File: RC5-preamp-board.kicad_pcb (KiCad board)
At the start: 2 copper layers, 69.8 x 48.3 mm, 28 parts, among them P1 RAW_DC, P10 CTL_OUT, P2 VCC, P201 FTDI Basic, P3 VCC, P4 VCC, P5 VCC, P6 VCC, P7 VCC, P8 INPUTS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

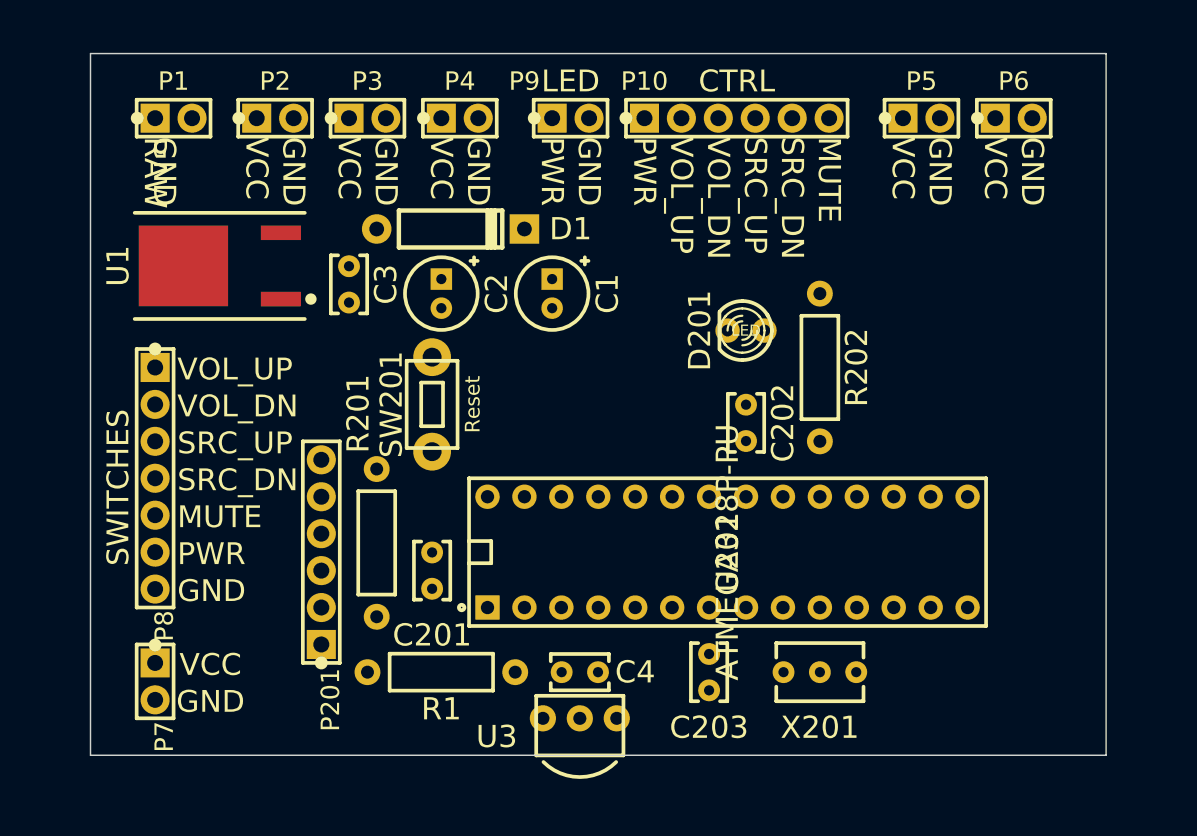
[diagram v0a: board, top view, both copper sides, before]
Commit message: Dimensioned and routed.
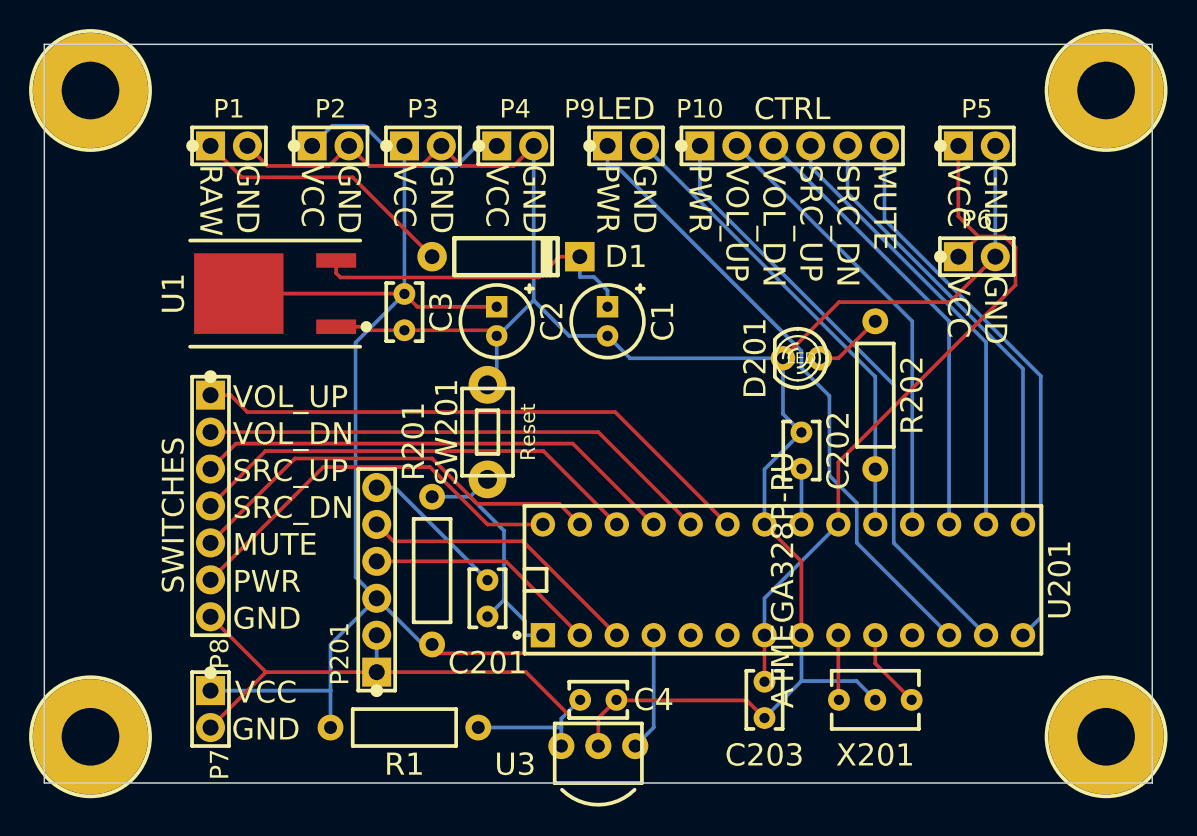
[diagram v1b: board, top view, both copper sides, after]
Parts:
- added mtg1: 4-40-PTH, mfk-MTG_4-40_0.156x0.312in, F.Cu at (104.8, 87.0)
- added mtg2: 4-40-PTH, mfk-MTG_4-40_0.156x0.312in, F.Cu at (174.6, 87.0)
- added mtg3: 4-40-PTH, mfk-MTG_4-40_0.156x0.312in, F.Cu at (174.6, 131.4)
- added mtg4: 4-40-PTH, mfk-MTG_4-40_0.156x0.312in, F.Cu at (104.8, 131.4)
- moved P6 9.86 mm to (165.7, 98.4)
- moved R1 4.58 mm to (126.4, 130.8)
- moved R201 4.26 mm to (128.3, 120.0)
- moved C1 4.26 mm to (140.3, 102.9)
- moved C2 4.26 mm to (132.7, 102.9)
- moved C201 4.26 mm to (132.1, 121.9)
- moved C203 4.26 mm to (151.1, 128.9)
- moved D1 4.26 mm to (133.3, 98.4)
- moved P1 4.26 mm to (114.3, 90.8)
- moved P10 4.26 mm to (153.0, 90.8)
- moved P2 4.26 mm to (121.3, 90.8)
- moved P3 4.26 mm to (127.6, 90.8)
- moved P4 4.26 mm to (134.0, 90.8)
- moved P5 4.26 mm to (165.7, 90.8)
- moved P9 4.26 mm to (141.6, 90.8)
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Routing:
- net DGND: track 0.00 -> 182.1 mm
- net /arduino-pcb/V_VCC: track 0.00 -> 161.0 mm
- net /arduino-pcb/D6: track 0.00 -> 43.7 mm
- net /arduino-pcb/D7: track 0.00 -> 41.8 mm
- net /arduino-pcb/A0: track 0.00 -> 39.2 mm
- net /arduino-pcb/D8: track 0.00 -> 38.6 mm
- net /arduino-pcb/A1: track 0.00 -> 35.7 mm
- net /arduino-pcb/A2: track 0.00 -> 33.5 mm
- net /arduino-pcb/SCK: track 0.00 -> 32.6 mm
- net /arduino-pcb/A3: track 0.00 -> 31.6 mm
- net /arduino-pcb/MOSI: track 0.00 -> 31.0 mm
- net /arduino-pcb/MISO: track 0.00 -> 31.0 mm
- net /arduino-pcb/D9: track 0.00 -> 31.0 mm
- net /arduino-pcb/D10: track 0.00 -> 31.0 mm
- net /arduino-pcb/A4: track 0.00 -> 29.7 mm
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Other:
- board size 69.8 x 48.3 mm -> 76.2 x 50.8 mm

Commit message: Shrunk and routed.
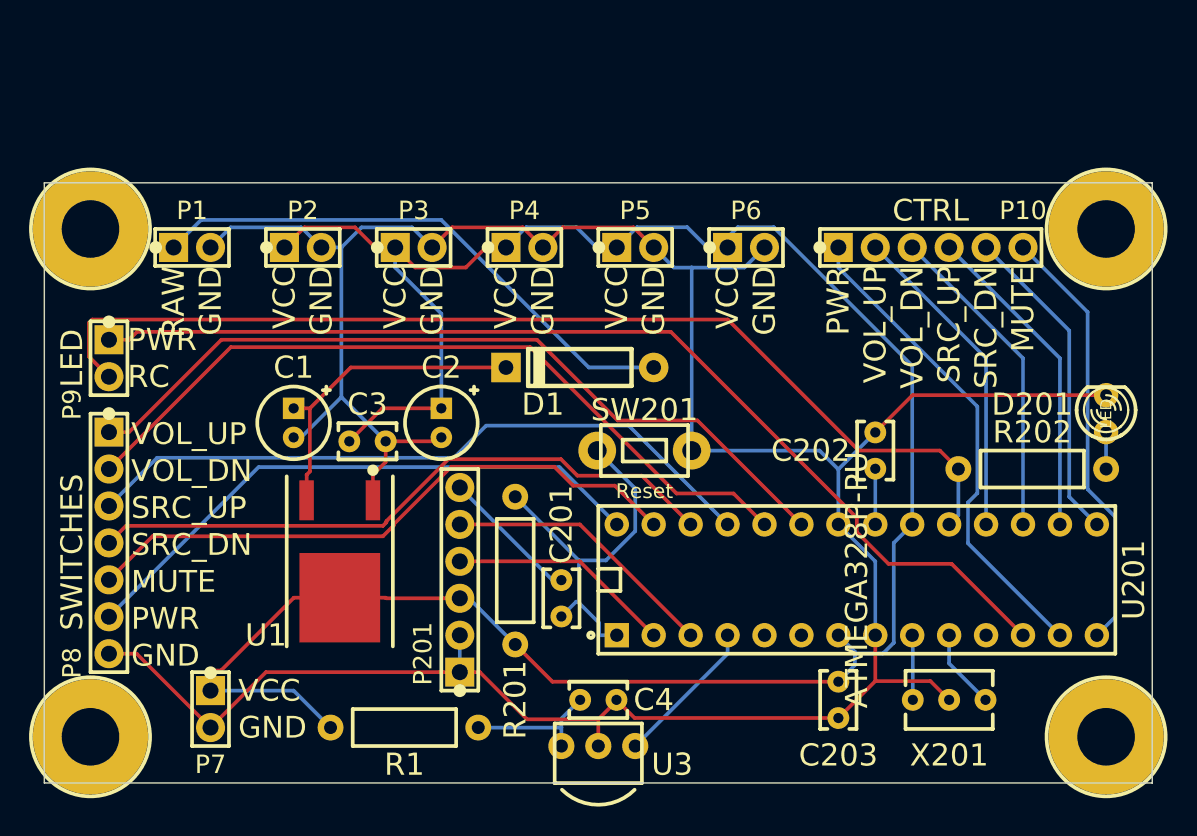
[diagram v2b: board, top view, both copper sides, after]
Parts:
- moved P9 38.4 mm to (106.0, 105.4), turned to 270 degrees
- moved P5 24.5 mm to (142.2, 97.8)
- moved C1 22.7 mm to (118.7, 109.9)
- moved D201 21.3 mm to (174.6, 109.2), turned to 90 degrees
- moved U1 18.9 mm to (121.9, 119.4), turned to 270 degrees
- moved P6 15.9 mm to (149.9, 97.8)
- moved R202 11.9 mm to (169.5, 113.0), turned to 0 degrees
- moved P10 11.8 mm to (162.6, 97.8)
- moved SW201 10.9 mm to (142.9, 111.8), turned to 0 degrees
- moved mtg1 9.52 mm to (104.8, 96.5)
- moved mtg2 9.52 mm to (174.6, 96.5)
- moved C3 9.25 mm to (123.8, 111.1), turned to 0 degrees
- moved D1 9.16 mm to (138.4, 106.0), turned to 180 degrees
- moved C2 7.96 mm to (128.9, 109.9)
- moved P8 7.43 mm to (106.0, 118.1)
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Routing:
- net /arduino-pcb/SCK: track 32.6 -> 72.5 mm
- net /arduino-pcb/D6: track 43.7 -> 72.3 mm
- net /RAW_DC: track 18.4 -> 38.0 mm
- net DGND: track 182.1 -> 200.4 mm
- net /arduino-pcb/A1: track 35.7 -> 53.6 mm
- net /arduino-pcb/A0: track 39.2 -> 55.5 mm
- net /arduino-pcb/A2: track 33.5 -> 47.6 mm
- net /arduino-pcb/A5: track 27.7 -> 40.8 mm
- net /arduino-pcb/A3: track 31.6 -> 44.3 mm
- net /arduino-pcb/A4: track 29.7 -> 42.4 mm
- net /arduino-pcb/D10: track 31.0 -> 22.2 mm
- net /arduino-pcb/MOSI: track 31.0 -> 22.2 mm
- net /arduino-pcb/MISO: track 31.0 -> 22.2 mm
- net /arduino-pcb/D9: track 31.0 -> 22.2 mm
- net /arduino-pcb/D8: track 38.6 -> 29.8 mm
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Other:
- board size 76.2 x 50.8 mm -> 76.2 x 41.3 mm
- board text added: "RC"

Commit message: Removed one VCC tap. Keystone 621 mtg added. Routed.
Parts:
- removed P7: VCC, mfk-SIL-2
- added VAL: REF, oshw-logo-150mil-FSilk, F.Cu at (144.8, 120.7)
- mtg1, mtg2, mtg3, mtg4: value 4-40-PTH -> 621; footprint mfk-MTG_4-40_0.156x0.312in -> mfk-KEYSTONE-621
- moved mtg3 69.8 mm to (104.8, 131.4)
- moved mtg4 69.8 mm to (174.6, 131.4)
- moved P6 49.0 mm to (113.0, 130.2), turned to 270 degrees
- moved D1 19.7 mm to (118.7, 105.4), turned to 0 degrees
- moved P2 3.81 mm to (123.2, 97.8)
- moved P3 3.81 mm to (130.8, 97.8)
- moved P4 3.81 mm to (138.4, 97.8)
- moved P5 3.81 mm to (146.1, 97.8)
- moved P1 3.81 mm to (115.6, 97.8)
- moved P10 2.54 mm to (160.0, 97.8)
- moved C202 1.80 mm to (157.5, 113.0), turned to 180 degrees
- moved SW201 1.42 mm to (144.1, 111.1)
- moved C203 1.42 mm to (157.5, 128.3), turned to 0 degrees
- moved R1 1.27 mm to (126.4, 132.1)
- moved P9 1.27 mm to (106.0, 104.1)
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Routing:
- net /arduino-pcb/V_VCC: track 157.7 -> 126.9 mm
- net /RAW_DC: track 38.0 -> 7.88 mm
- net DGND: track 200.4 -> 190.6 mm
- net N-0000026: track 22.2 -> 13.4 mm
- net /arduino-pcb/A4: track 42.4 -> 49.4 mm
- net /arduino-pcb/A3: track 44.3 -> 50.9 mm
- net /arduino-pcb/A2: track 47.6 -> 52.8 mm
- net /arduino-pcb/DTR: track 9.62 -> 13.6 mm
- net /arduino-pcb/A1: track 53.6 -> 49.7 mm
- net /arduino-pcb/A0: track 55.5 -> 53.3 mm
- net /arduino-pcb/RESET: track 26.1 -> 28.1 mm
- net /arduino-pcb/D10: track 22.2 -> 23.3 mm
- net /arduino-pcb/MOSI: track 22.2 -> 23.3 mm
- net /arduino-pcb/MISO: track 22.2 -> 23.3 mm
- net /arduino-pcb/D9: track 22.2 -> 23.3 mm
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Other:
- board text added: "1.0"
- board text added: "CERN Open Hardware License v1.2"
- board text added: "Copyright (C) 2015 Mithat Konar"
- board text added: "PreampControl"

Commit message: Silk tweaks.
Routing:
- added copper zone on F.Cu, net DGND
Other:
- board text added: "Reset"
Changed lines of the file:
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@@
     (area 97.837172 76.099999 192.455715 147.48)
     (thickness 1.6)
-    (drawings 53)
+    (drawings 54)
     (tracks 205)
     (zones 0)
@@
     (visible_elements 7FFFFFFF)
     (pcbplotparams
-      (layerselection 3178497)
+      (layerselection 283148289)
       (usegerberextensions true)
       (excludeedgelayer true)
-      (linewidth 0.150000)
+      (linewidth 0.152400)
       (plotframeref false)
       (viasonmask false)
@@
       (psa4output false)
       (plotreference true)
-      (plotvalue true)
+      (plotvalue false)
       (plotothertext true)
       (plotinvisibletext false)
@@
       (outputformat 1)
       (mirror false)
-      (drillshape 1)
+      (drillshape 0)
       (scaleselection 1)
-      (outputdirectory ""))
+      (outputdirectory Gerbers))
   )
   (net 0 "")
@@
       (effects (font (size 1.524 1.524) (thickness 0.1524)))
     )
-    (fp_text value Reset (at 0 -2.794) (layer F.SilkS)
+    (fp_text value Reset (at 0 0) (layer F.SilkS)
       (effects (font (size 1.524 1.524) (thickness 0.1524)))
     )
@@
     (descr "2-pin SIL")
     (tags "CONN DEV SIL Jumper")
-    (fp_text reference P9 (at 3.175 2.54 270) (layer F.SilkS)
+    (fp_text reference P9 (at 3.429 2.54 270) (layer F.SilkS)
       (effects (font (size 1.27 1.27) (thickness 0.127)))
     )
@@
     (tags "DPAK TO-252 TO228P1003X238-3N IPC-7351")
     (attr smd)
-    (fp_text reference U1 (at 5.08 5.08 360) (layer F.SilkS)
+    (fp_text reference U1 (at 7.62 0 360) (layer F.SilkS)
       (effects (font (size 1.524 1.524) (thickness 0.1524)))
     )
@@
       (xy 1.47828 -0.47244)) (layer F.SilkS) (width 0.00254))
   )
+  (gr_text Reset (at 144.145 108.331) (layer F.SilkS)
+    (effects (font (size 1.524 1.524) (thickness 0.1524)))
+  )
   (gr_text "CERN Open Hardware License v1.2" (at 147.32 120.65) (layer F.SilkS)
     (effects (font (size 1.524 1.016) (thickness 0.254)) (justify left))
@@
   (segment (start 161.29 124.46) (end 161.33 124.5) (width 0.254) (layer B.Cu) (net 27))
   (segment (start 174.625 110.49) (end 174.625 113.03) (width 0.254) (layer B.Cu) (net 28))
+  (zone (net 23) (net_name DGND) (layer F.Cu) (hatch edge 0.508)
+    (connect_pads (clearance 0.508))
+    (min_thickness 0.2032)
+    (fill (arc_segments 16) (thermal_gap 0.508) (thermal_bridge_width 0.254))
+    (polygon
+      (pts
+        (xy 177.8 134.62) (xy 101.6 134.62) (xy 101.6 93.345) (xy 177.8 93.345)
+      )
+    )
+  )
 )

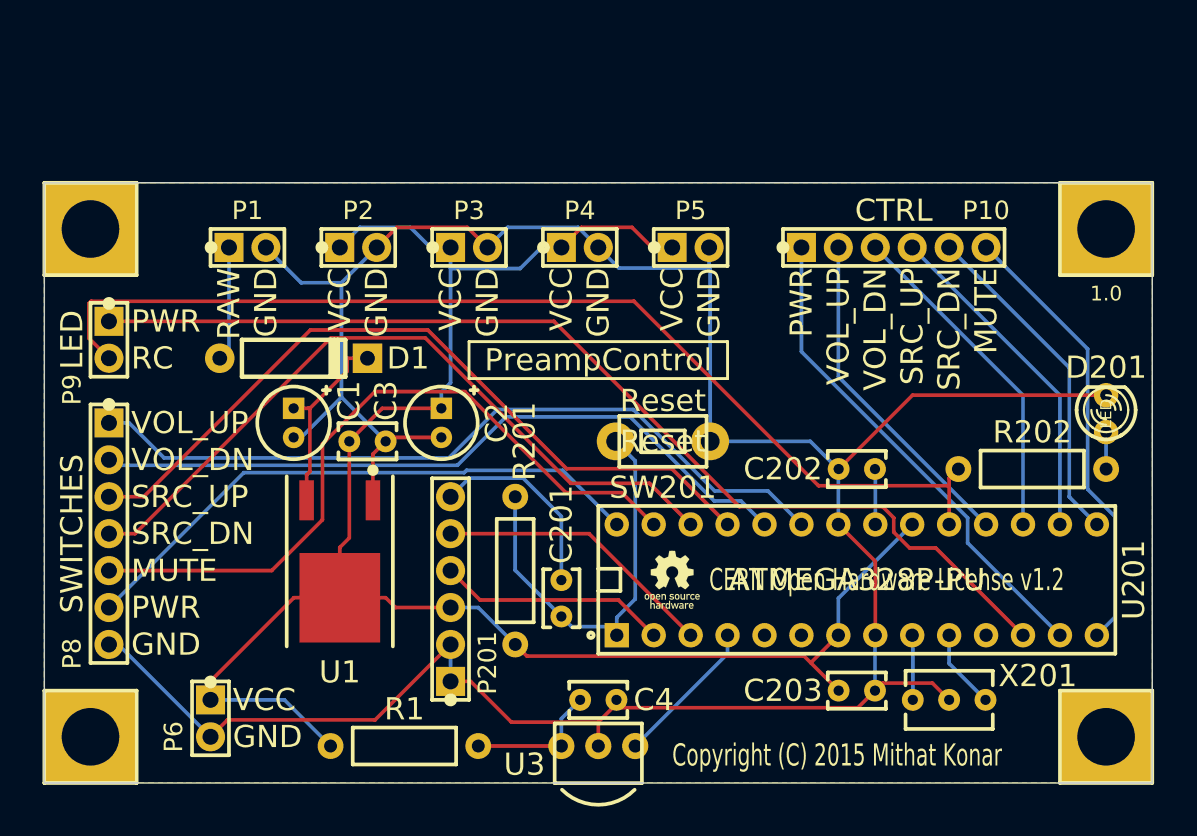
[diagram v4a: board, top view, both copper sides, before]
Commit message: Nudged TSOP receiver back so the main body is just a hair recessed from PCB edge.
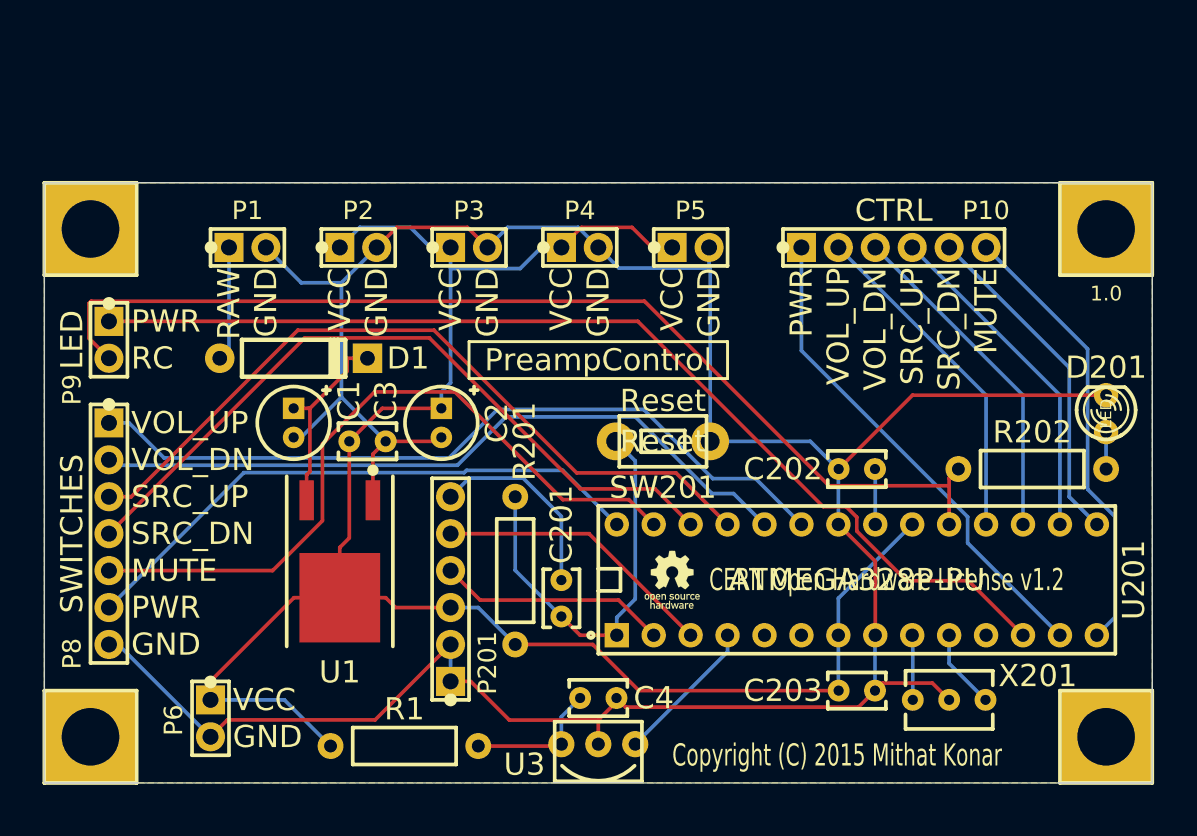
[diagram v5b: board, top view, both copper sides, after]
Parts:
- U3: footprint mfk-Vishay-TSOP341xx -> mfk-Vishay-TSOP341xx-alt
- moved C4 0.13 mm to (139.7, 128.8)
- moved U3 0.13 mm to (139.7, 132.0)
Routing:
- net /arduino-pcb/V_VCC: track 126.9 -> 128.1 mm

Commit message: Moved module to right side of board.
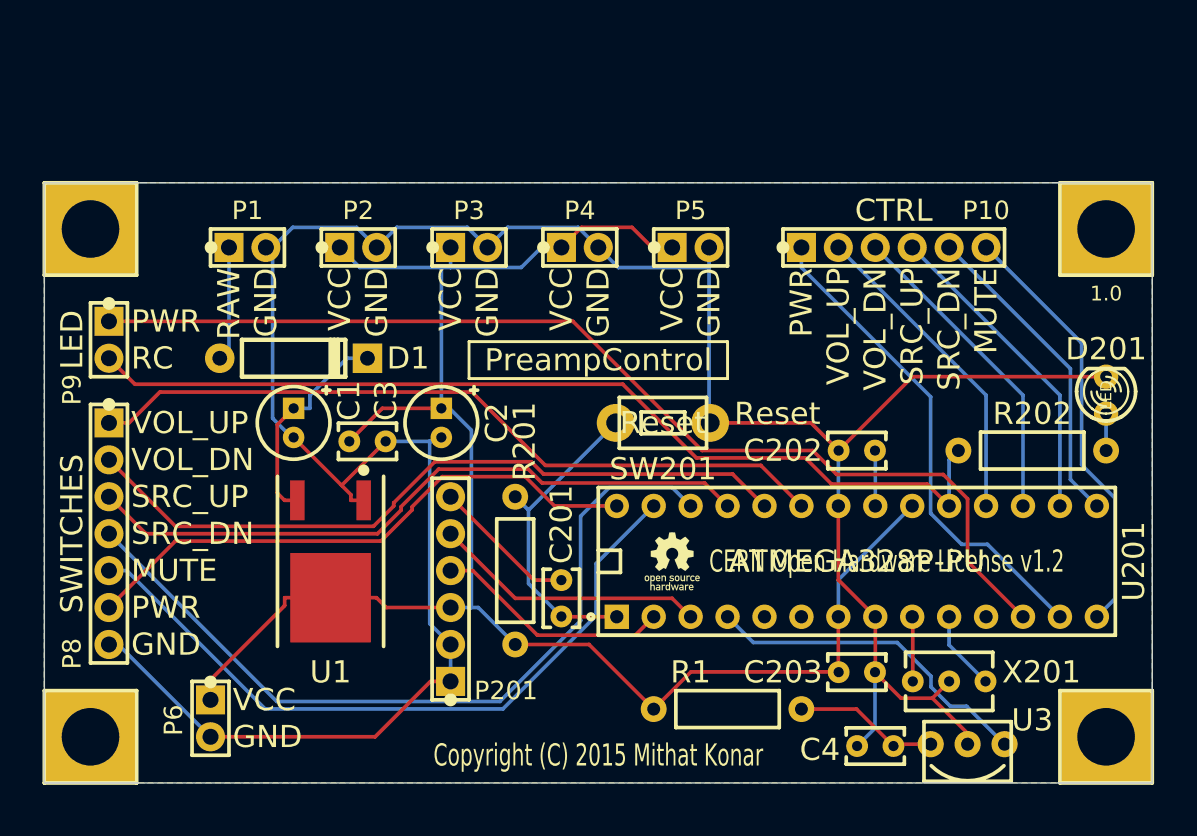
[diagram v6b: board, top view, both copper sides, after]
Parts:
- moved U3 25.4 mm to (165.1, 132.0)
- moved R1 22.4 mm to (148.6, 129.5)
- moved C4 19.3 mm to (158.8, 132.1), turned to 180 degrees
- moved C203 1.27 mm to (157.5, 127.0)
- moved U201 1.27 mm to (157.5, 119.4)
- moved VAL 1.27 mm to (144.8, 119.4)
- moved C202 1.27 mm to (157.5, 111.8)
- moved D201 1.27 mm to (174.6, 108.0)
- moved R202 1.27 mm to (169.5, 111.8)
- moved SW201 1.27 mm to (144.1, 109.9)
- moved X201 1.27 mm to (163.8, 127.6)
- moved U1 0.64 mm to (121.3, 119.4)
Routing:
- net /arduino-pcb/D2: track 10.1 -> 23.1 mm
- net DGND: track 190.6 -> 182.7 mm
- net /arduino-pcb/SCK: track 72.9 -> 66.1 mm
- net /arduino-pcb/RESET: track 28.3 -> 21.8 mm
- net /arduino-pcb/A2: track 52.8 -> 46.6 mm
- net /arduino-pcb/A3: track 50.9 -> 55.6 mm
- net /arduino-pcb/V_VCC: track 128.1 -> 123.6 mm
- net /arduino-pcb/DTR: track 13.6 -> 10.00 mm
- net /arduino-pcb/A0: track 53.3 -> 51.7 mm
- net N-0000026: track 13.4 -> 14.9 mm
- net /arduino-pcb/D6: track 72.4 -> 73.8 mm
- net /arduino-pcb/MOSI: track 23.3 -> 22.0 mm
- net /arduino-pcb/MISO: track 23.3 -> 22.0 mm
- net /arduino-pcb/D10: track 23.3 -> 22.0 mm
- net /arduino-pcb/D9: track 23.3 -> 22.0 mm
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- added copper zone on B.Cu, net DGND
- removed copper zone on F.Cu, net DGND
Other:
- board text added: "blk"
- board text added: "gnd"
- board text added: "grn"
- board text added: "rxi"
- board text added: "txo"
- board text added: "vcc"
